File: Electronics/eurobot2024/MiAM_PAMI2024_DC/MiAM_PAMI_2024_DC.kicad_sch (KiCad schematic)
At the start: 31 parts, among them J1 Conn_01x02_Pin, J2 Conn_01x02_Pin, J3 Conn_01x02_Pin, SW1 SW_DPDT_x2, U1 ESP32-DEVKITC-32U, U2 3V3, U4 5V, U6 TB6612FNG, U9 MT3608

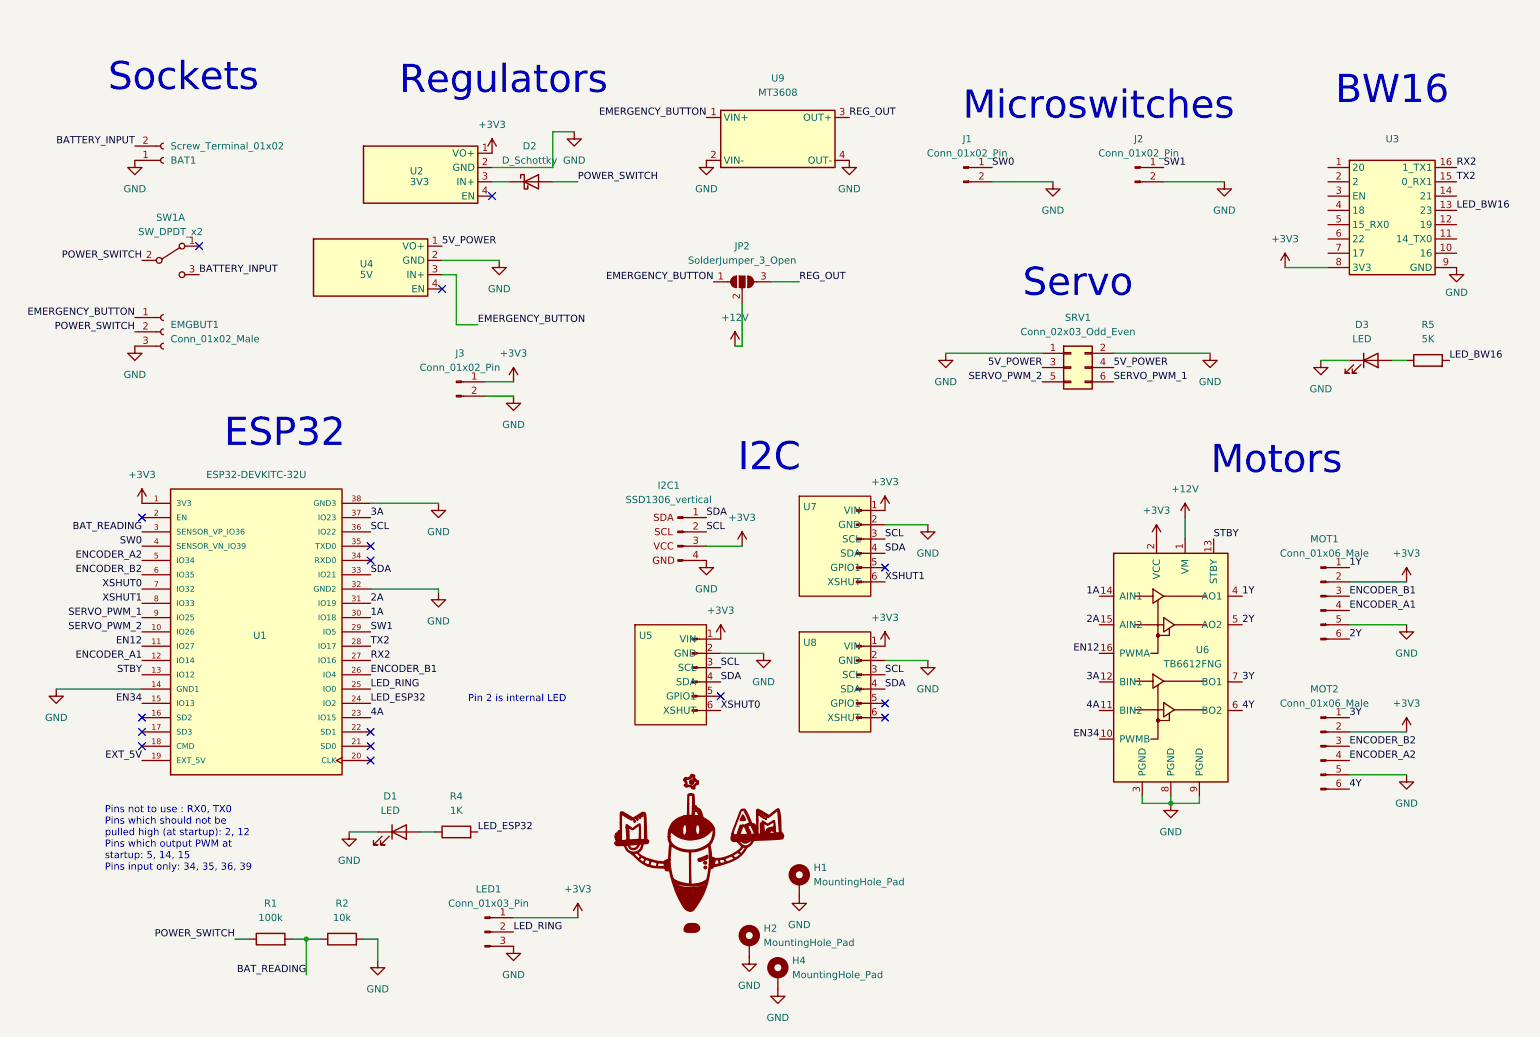
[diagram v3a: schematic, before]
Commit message: Add additional breakout for BW16
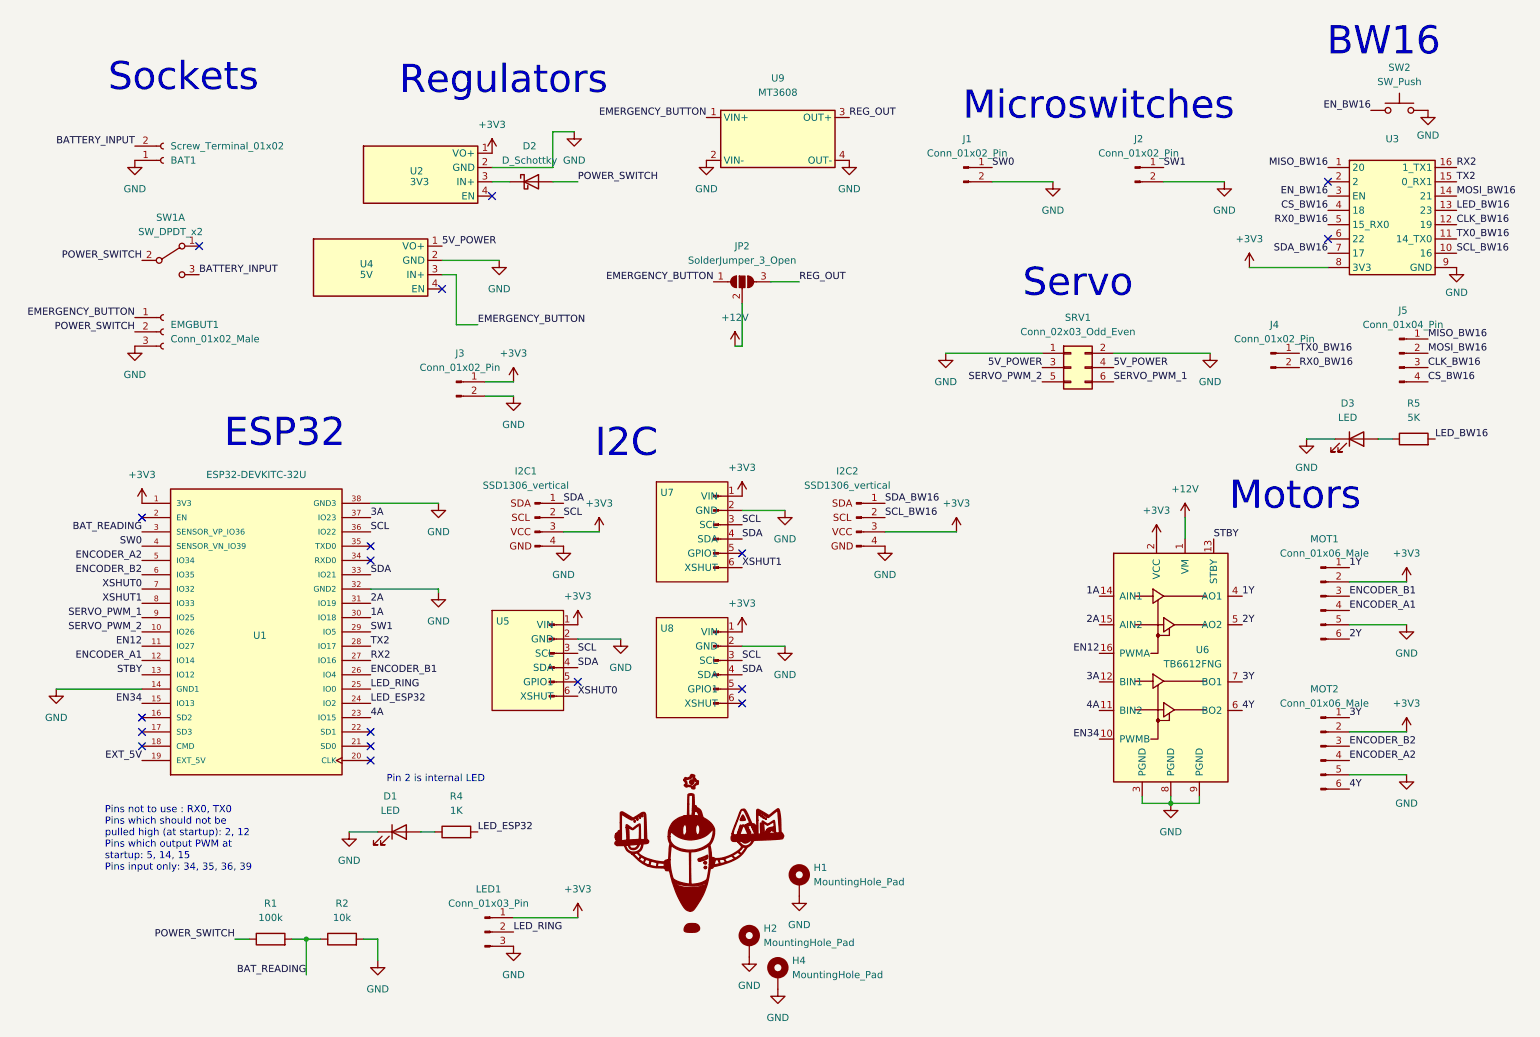
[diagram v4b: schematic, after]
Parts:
- added I2C2: SSD1306_vertical, Connector_PinHeader_2.54mm:PinHeader_1x04_P2.54mm_Vertical, symbol MiAM_ESP32:SSD1306_vertical
- added J4: Conn_01x02_Pin, Connector_PinHeader_2.54mm:PinHeader_1x02_P2.54mm_Vertical, symbol Connector:Conn_01x02_Pin
- added J5: Conn_01x04_Pin, Connector_PinHeader_2.54mm:PinHeader_1x04_P2.54mm_Vertical, symbol Connector:Conn_01x04_Pin
- added SW2: SW_Push, Button_Switch_SMD:SW_Push_1P1T_NO_Vertical_Wuerth_434133025816, symbol Switch:SW_Push
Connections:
- net +3V3: now also I2C2.3 (VCC)
- net GND: now also I2C2.4 (GND), SW2.2
- net MISO_BW16: now reaches U3.1 (20)
- net MISO_BW16: now also J5.1 (Pin_1)
- net SCL_BW16: now reaches U3.10 (16)
- net SCL_BW16: now also I2C2.2 (SCL)
- net TX0_BW16: now reaches U3.11 (14_TX0)
- net TX0_BW16: now also J4.1 (Pin_1)
- net CLK_BW16: now reaches U3.12 (19)
- net CLK_BW16: now also J5.3 (Pin_3)
- net MOSI_BW16: now reaches U3.14 (21)
- net MOSI_BW16: now also J5.2 (Pin_2)
- net EN_BW16: now reaches U3.3 (EN)
- net EN_BW16: now also SW2.1
- net CS_BW16: now reaches U3.4 (18)
- net CS_BW16: now also J5.4 (Pin_4)
- net RX0_BW16: now reaches U3.5 (15_RX0)
- net RX0_BW16: now also J4.2 (Pin_2)
- net SDA_BW16: now reaches U3.7 (17)
- net SDA_BW16: now also I2C2.1 (SDA)
- no-connect marks 16 -> 18
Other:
- moved on the sheet: D3, I2C1, R5, U5, U7, U8
